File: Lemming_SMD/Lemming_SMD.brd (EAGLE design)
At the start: 45.7 x 50.8 mm, 35 parts, among them Q1 2SA1203, Q11 SS8050, Q12 2SA1203, Q2 SS8050, Q3 2SA1203, Q4 SS8050, Q5 2SA1203, Q6 SS8050, U3 BME280, X1 I2C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

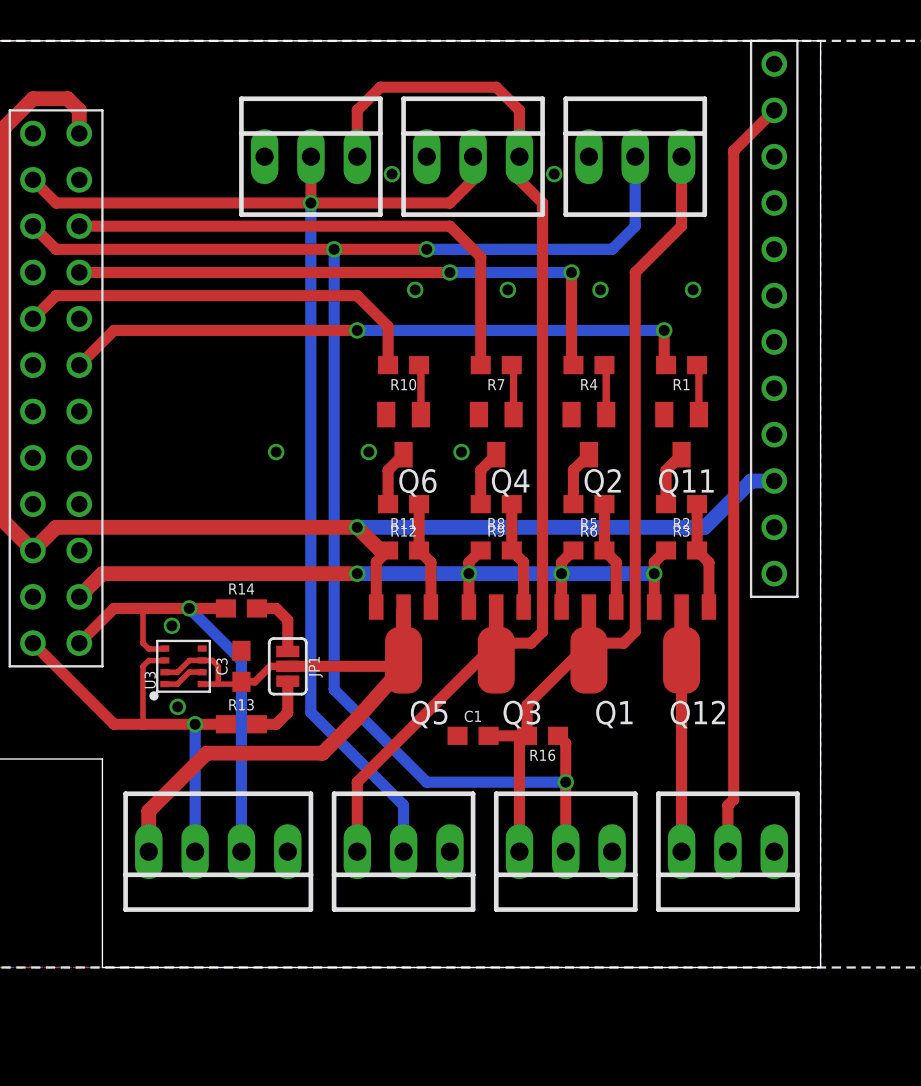
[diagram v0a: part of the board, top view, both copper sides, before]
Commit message: Ordered Version 1.0 from Seeed
Lemming_SMD V1.0
Lagopus_A V1.0
Lagopus_B V1.0
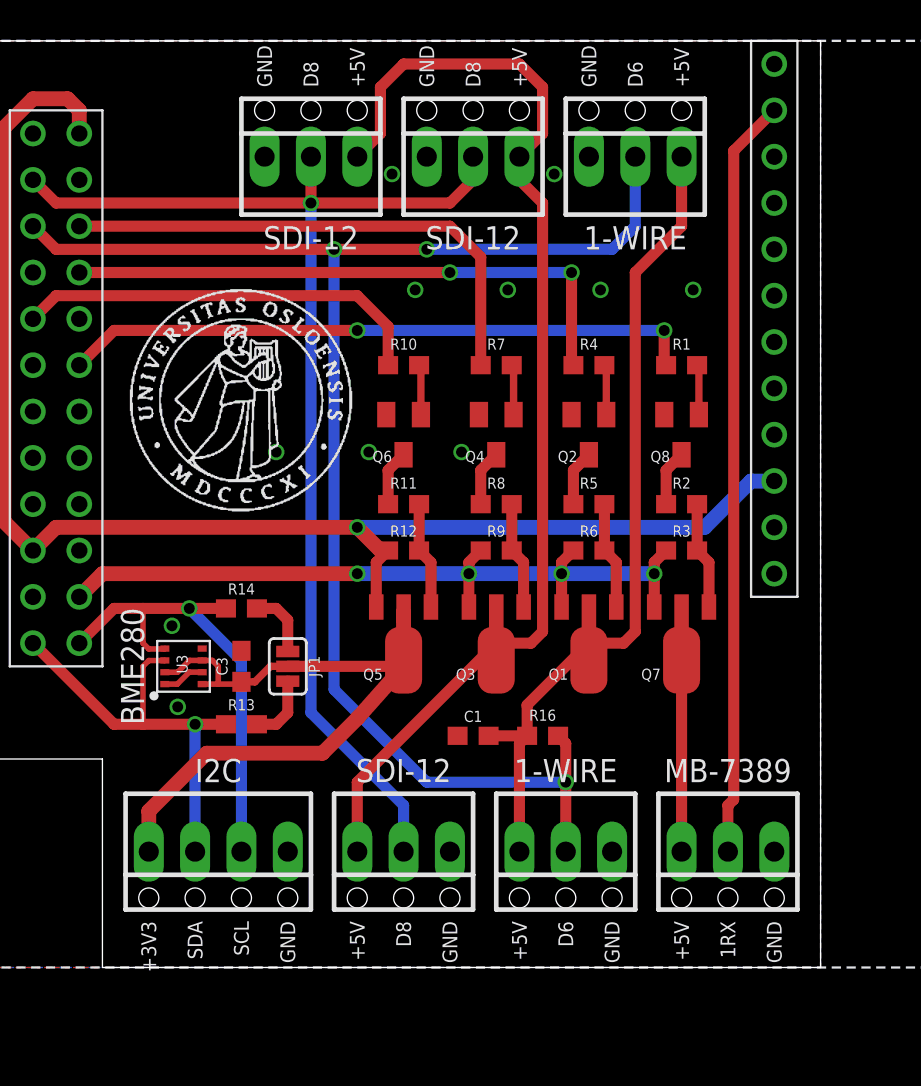
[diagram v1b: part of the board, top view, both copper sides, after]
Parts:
- added U$3: (no value), UIO-John:UIO-LOGO-BL
- Q1, Q3, Q5, Q7: value 2SA1203 -> 2STF2360
- renumbered Q11 to Q8, Q12 to Q7
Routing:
- net 5V_D7: track 60.7 -> 64.3 mm
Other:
- board text added: "(C) 2018 john.hulth@geo.uio.no"
- board text added: "+3V3"
- board text added: "Lemming SMD V1.0"
- board text removed: "(C)john.hulth@geo.uio.no 2018"
- board text removed: "+3.3V"
- board text removed: "Lemming Sensor board V1.0"

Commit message: Lemming SMD new order 2020
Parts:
- JP1: value (none) -> JUMPER-SMT_3_NO_SILK; device SparkFun-Jumpers:SMT-JUMPER_3_2-NC_PASTE_SILK -> SparkFun-Jumpers:SMT-JUMPER_3_NO_SILK

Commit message: Minor changes befor order
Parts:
- added X8: IRIDIUM, con-molex:22-23-2031
- added X9: IRIDIUM-2, con-molex:22-23-2031
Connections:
- net 2RX: now also X8.1
- net 2TX: now also X8.2
- net BATTERY: now also X9.1
- net D4: now also X8.3
- net GND: now also X9.2, X9.3
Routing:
- net D4: track 0.00 -> 89.9 mm
- net BATTERY: track 0.00 -> 36.0 mm
- net 2TX: track 0.00 -> 32.5 mm
- net 2RX: track 0.00 -> 32.5 mm
- net 3V3_SENS: track 78.0 -> 47.8 mm
- net GND: vias 11 -> 15
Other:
- board size 45.7 x 50.8 mm -> 55.2 x 50.8 mm
- board text added: "(C) 2020 john.hulth@geo.uio.no"
- board text added: "2RX"
- board text added: "2TX"
- board text added: "BAT"
- board text added: "D4"
- board text added: "Lemming SMD V1.1"
- board text added: "X12"
- board text added: "X24"
- board text removed: "(C) 2018 john.hulth@geo.uio.no"
- board text removed: "Lemming SMD V1.0"
